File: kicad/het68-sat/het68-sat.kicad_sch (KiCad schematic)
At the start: 10 parts, among them J1 RJ45, U1 AP2112K-1.8

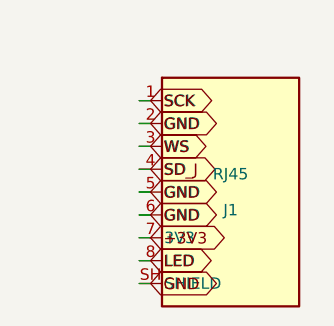
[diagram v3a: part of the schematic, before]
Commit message: Shrink the acoustic board and ground the cable shield only at the HAT.
The HAT outline is 94 by 96 mm and the satellite shell pin is open. The README drops the power-board LED note and estimates a self-built Pico Plus 2 W against the bought module.

Co-authored-by: Cursor <cursoragent@cursor.com>
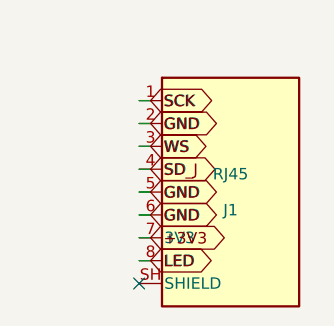
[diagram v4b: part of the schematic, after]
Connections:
- net GND: no longer J1.SH (SHIELD)
- no-connect marks 4 -> 5
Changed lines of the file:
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@@
     (property "Datasheet" "" (at 20 30 0) (effects (font (size 1.27 1.27)) (hide yes)))
     (pin "1")
-    (instances (project "het68-sat" (path "/bc35c63d-5e56-4895-a755-860cebd8b63c" (reference "#PWR00") (unit 1))))
+    (instances (project "het68-sat" (path "/c4451ac6-91a4-4f15-b70a-fef6d342434a" (reference "#PWR00") (unit 1))))
   )
   (global_label "GND"
@@
     (property "Datasheet" "" (at 20 45 0) (effects (font (size 1.27 1.27)) (hide yes)))
     (pin "1")
-    (instances (project "het68-sat" (path "/bc35c63d-5e56-4895-a755-860cebd8b63c" (reference "#PWR01") (unit 1))))
+    (instances (project "het68-sat" (path "/c4451ac6-91a4-4f15-b70a-fef6d342434a" (reference "#PWR01") (unit 1))))
   )
   (global_label "+3V3A"
@@
     (property "Datasheet" "" (at 20 60 0) (effects (font (size 1.27 1.27)) (hide yes)))
     (pin "1")
-    (instances (project "het68-sat" (path "/bc35c63d-5e56-4895-a755-860cebd8b63c" (reference "#PWR02") (unit 1))))
+    (instances (project "het68-sat" (path "/c4451ac6-91a4-4f15-b70a-fef6d342434a" (reference "#PWR02") (unit 1))))
   )
   (global_label "VSYS"
@@
     (property "Datasheet" "" (at 20 75 0) (effects (font (size 1.27 1.27)) (hide yes)))
     (pin "1")
-    (instances (project "het68-sat" (path "/bc35c63d-5e56-4895-a755-860cebd8b63c" (reference "#PWR03") (unit 1))))
+    (instances (project "het68-sat" (path "/c4451ac6-91a4-4f15-b70a-fef6d342434a" (reference "#PWR03") (unit 1))))
   )
   (global_label "VBUS"
@@
     (property "Datasheet" "" (at 20 90 0) (effects (font (size 1.27 1.27)) (hide yes)))
     (pin "1")
-    (instances (project "het68-sat" (path "/bc35c63d-5e56-4895-a755-860cebd8b63c" (reference "#PWR04") (unit 1))))
+    (instances (project "het68-sat" (path "/c4451ac6-91a4-4f15-b70a-fef6d342434a" (reference "#PWR04") (unit 1))))
   )
   (global_label "+3V3"
@@
     (pin "8")
     (pin "SH")
-    (instances (project "het68-sat" (path "/bc35c63d-5e56-4895-a755-860cebd8b63c" (reference "J1") (unit 1))))
+    (instances (project "het68-sat" (path "/c4451ac6-91a4-4f15-b70a-fef6d342434a" (reference "J1") (unit 1))))
   )
   (wire (pts (xy 29.84 489.84) (xy 31.11 489.84))
@@
     (effects (font (size 1.27 1.27)) (justify left))
   )
-  (wire (pts (xy 29.84 510.16) (xy 31.11 510.16))
-    (stroke (width 0) (type solid)))
-  (global_label "GND"
-    (shape bidirectional)
-    (at 31.11 510.16 0)
-    (effects (font (size 1.27 1.27)) (justify left))
-  )
+  (no_connect (at 29.84 510.16))
   (symbol
     (lib_id "het68:AP2112K-1.8")
@@
     (pin "4")
     (pin "5")
-    (instances (project "het68-sat" (path "/bc35c63d-5e56-4895-a755-860cebd8b63c" (reference "U1") (unit 1))))
+    (instances (project "het68-sat" (path "/c4451ac6-91a4-4f15-b70a-fef6d342434a" (reference "U1") (unit 1))))
   )
   (wire (pts (xy 31.11 459.14) (xy 32.38 459.14))
@@
     (pin "4")
     (pin "5")
-    (instances (project "het68-sat" (path "/bc35c63d-5e56-4895-a755-860cebd8b63c" (reference "MK1") (unit 1))))
+    (instances (project "het68-sat" (path "/c4451ac6-91a4-4f15-b70a-fef6d342434a" (reference "MK1") (unit 1))))
   )
   (wire (pts (xy 31.11 433.52) (xy 32.38 433.52))
@@
     (pin "3")
     (pin "4")
-    (instances (project "het68-sat" (path "/bc35c63d-5e56-4895-a755-860cebd8b63c" (reference "D1") (unit 1))))
+    (instances (project "het68-sat" (path "/c4451ac6-91a4-4f15-b70a-fef6d342434a" (reference "D1") (unit 1))))
   )
   (wire (pts (xy 40.0 402.82) (xy 40.0 404.09))
@@
     (pin "1")
     (pin "2")
-    (instances (project "het68-sat" (path "/bc35c63d-5e56-4895-a755-860cebd8b63c" (reference "C1") (unit 1))))
+    (instances (project "het68-sat" (path "/c4451ac6-91a4-4f15-b70a-fef6d342434a" (reference "C1") (unit 1))))
   )
   (wire (pts (xy 40.0 373.39) (xy 40.0 374.66))
@@
     (pin "1")
     (pin "2")
-    (instances (project "het68-sat" (path "/bc35c63d-5e56-4895-a755-860cebd8b63c" (reference "C2") (unit 1))))
+    (instances (project "het68-sat" (path "/c4451ac6-91a4-4f15-b70a-fef6d342434a" (reference "C2") (unit 1))))
   )
   (wire (pts (xy 40.0 347.77) (xy 40.0 349.04))
@@
     (pin "1")
     (pin "2")
-    (instances (project "het68-sat" (path "/bc35c63d-5e56-4895-a755-860cebd8b63c" (reference "C3") (unit 1))))
+    (instances (project "het68-sat" (path "/c4451ac6-91a4-4f15-b70a-fef6d342434a" (reference "C3") (unit 1))))
   )
   (wire (pts (xy 40.0 322.15) (xy 40.0 323.42))
@@
     (pin "1")
     (pin "2")
-    (instances (project "het68-sat" (path "/bc35c63d-5e56-4895-a755-860cebd8b63c" (reference "C4") (unit 1))))
+    (instances (project "het68-sat" (path "/c4451ac6-91a4-4f15-b70a-fef6d342434a" (reference "C4") (unit 1))))
   )
   (wire (pts (xy 40.0 296.53) (xy 40.0 297.8))
@@
     (pin "1")
     (pin "2")
-    (instances (project "het68-sat" (path "/bc35c63d-5e56-4895-a755-860cebd8b63c" (reference "R1") (unit 1))))
+    (instances (project "het68-sat" (path "/c4451ac6-91a4-4f15-b70a-fef6d342434a" (reference "R1") (unit 1))))
   )
   (wire (pts (xy 40.0 270.91) (xy 40.0 272.18))
@@
     (pin "1")
     (pin "2")
-    (instances (project "het68-sat" (path "/bc35c63d-5e56-4895-a755-860cebd8b63c" (reference "R2") (unit 1))))
+    (instances (project "het68-sat" (path "/c4451ac6-91a4-4f15-b70a-fef6d342434a" (reference "R2") (unit 1))))
   )
   (wire (pts (xy 40.0 245.29) (xy 40.0 246.56))

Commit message: Fit every board on printed.cz prototype: 2-layer, 0603, ENIG.
HAT is 140×140 mm so it routes on two layers without 0402 or BGA; satellite and power use the same stack, drill and finish.

Co-authored-by: Cursor <cursoragent@cursor.com>
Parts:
- C1, C2: footprint Capacitor_SMD:C_0402_1005Metric -> Capacitor_SMD:C_0603_1608Metric; MPN CL05A105KA5NQNC -> CL10A105KA8NNNC
- C3, C4: footprint Capacitor_SMD:C_0402_1005Metric -> Capacitor_SMD:C_0603_1608Metric; MPN CL05B104KB5NNNC -> CL10B104KB8NNNC
- R1: footprint Resistor_SMD:R_0402_1005Metric -> Resistor_SMD:R_0603_1608Metric; MPN RC0402FR-0733RL -> RC0603FR-0733RL
- R2: footprint Resistor_SMD:R_0402_1005Metric -> Resistor_SMD:R_0603_1608Metric; MPN RC0402FR-07100KL -> RC0603FR-07100KL
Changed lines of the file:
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@@
     (property "Datasheet" "" (at 20 30 0) (effects (font (size 1.27 1.27)) (hide yes)))
     (pin "1")
-    (instances (project "het68-sat" (path "/2236da0a-ab6f-4773-9c91-a66ce1ab8b2c" (reference "#PWR00") (unit 1))))
+    (instances (project "het68-sat" (path "/938f7ccd-ed1f-4e5b-b71f-bcb60b7c252a" (reference "#PWR00") (unit 1))))
   )
   (global_label "GND"
@@
     (property "Datasheet" "" (at 20 45 0) (effects (font (size 1.27 1.27)) (hide yes)))
     (pin "1")
-    (instances (project "het68-sat" (path "/2236da0a-ab6f-4773-9c91-a66ce1ab8b2c" (reference "#PWR01") (unit 1))))
+    (instances (project "het68-sat" (path "/938f7ccd-ed1f-4e5b-b71f-bcb60b7c252a" (reference "#PWR01") (unit 1))))
   )
   (global_label "+3V3A"
@@
     (property "Datasheet" "" (at 20 60 0) (effects (font (size 1.27 1.27)) (hide yes)))
     (pin "1")
-    (instances (project "het68-sat" (path "/2236da0a-ab6f-4773-9c91-a66ce1ab8b2c" (reference "#PWR02") (unit 1))))
+    (instances (project "het68-sat" (path "/938f7ccd-ed1f-4e5b-b71f-bcb60b7c252a" (reference "#PWR02") (unit 1))))
   )
   (global_label "VSYS"
@@
     (property "Datasheet" "" (at 20 75 0) (effects (font (size 1.27 1.27)) (hide yes)))
     (pin "1")
-    (instances (project "het68-sat" (path "/2236da0a-ab6f-4773-9c91-a66ce1ab8b2c" (reference "#PWR03") (unit 1))))
+    (instances (project "het68-sat" (path "/938f7ccd-ed1f-4e5b-b71f-bcb60b7c252a" (reference "#PWR03") (unit 1))))
   )
   (global_label "VBUS"
@@
     (property "Datasheet" "" (at 20 90 0) (effects (font (size 1.27 1.27)) (hide yes)))
     (pin "1")
-    (instances (project "het68-sat" (path "/2236da0a-ab6f-4773-9c91-a66ce1ab8b2c" (reference "#PWR04") (unit 1))))
+    (instances (project "het68-sat" (path "/938f7ccd-ed1f-4e5b-b71f-bcb60b7c252a" (reference "#PWR04") (unit 1))))
   )
   (global_label "+3V3"
@@
     (pin "8")
     (pin "SH")
-    (instances (project "het68-sat" (path "/2236da0a-ab6f-4773-9c91-a66ce1ab8b2c" (reference "J1") (unit 1))))
+    (instances (project "het68-sat" (path "/938f7ccd-ed1f-4e5b-b71f-bcb60b7c252a" (reference "J1") (unit 1))))
   )
   (wire (pts (xy 29.84 489.84) (xy 31.11 489.84))
@@
     (pin "4")
     (pin "5")
-    (instances (project "het68-sat" (path "/2236da0a-ab6f-4773-9c91-a66ce1ab8b2c" (reference "U1") (unit 1))))
+    (instances (project "het68-sat" (path "/938f7ccd-ed1f-4e5b-b71f-bcb60b7c252a" (reference "U1") (unit 1))))
   )
   (wire (pts (xy 31.11 459.14) (xy 32.38 459.14))
@@
     (pin "4")
     (pin "5")
-    (instances (project "het68-sat" (path "/2236da0a-ab6f-4773-9c91-a66ce1ab8b2c" (reference "MK1") (unit 1))))
+    (instances (project "het68-sat" (path "/938f7ccd-ed1f-4e5b-b71f-bcb60b7c252a" (reference "MK1") (unit 1))))
   )
   (wire (pts (xy 31.11 433.52) (xy 32.38 433.52))
@@
     (pin "3")
     (pin "4")
-    (instances (project "het68-sat" (path "/2236da0a-ab6f-4773-9c91-a66ce1ab8b2c" (reference "D1") (unit 1))))
+    (instances (project "het68-sat" (path "/938f7ccd-ed1f-4e5b-b71f-bcb60b7c252a" (reference "D1") (unit 1))))
   )
   (wire (pts (xy 40.0 402.82) (xy 40.0 404.09))
@@
     (property "Reference" "C1" (at 40.0 379.2 0) (effects (font (size 1.27 1.27))))
     (property "Value" "1u" (at 40.0 375.2 0) (effects (font (size 1.27 1.27))))
-    (property "Footprint" "Capacitor_SMD:C_0402_1005Metric" (at 40.0 377.2 0) (effects (font (size 1.27 1.27)) (hide yes)))
+    (property "Footprint" "Capacitor_SMD:C_0603_1608Metric" (at 40.0 377.2 0) (effects (font (size 1.27 1.27)) (hide yes)))
     (property "Datasheet" "" (at 40.0 377.2 0) (effects (font (size 1.27 1.27)) (hide yes)))
-    (property "MPN" "CL05A105KA5NQNC" (at 40.0 377.2 0) (effects (font (size 1.27 1.27)) (hide yes)))
-    (pin "1")
-    (pin "2")
-    (instances (project "het68-sat" (path "/2236da0a-ab6f-4773-9c91-a66ce1ab8b2c" (reference "C1") (unit 1))))
+    (property "MPN" "CL10A105KA8NNNC" (at 40.0 377.2 0) (effects (font (size 1.27 1.27)) (hide yes)))
+    (pin "1")
+    (pin "2")
+    (instances (project "het68-sat" (path "/938f7ccd-ed1f-4e5b-b71f-bcb60b7c252a" (reference "C1") (unit 1))))
   )
   (wire (pts (xy 40.0 373.39) (xy 40.0 374.66))
@@
     (property "Reference" "C2" (at 40.0 353.58 0) (effects (font (size 1.27 1.27))))
     (property "Value" "1u" (at 40.0 349.58 0) (effects (font (size 1.27 1.27))))
-    (property "Footprint" "Capacitor_SMD:C_0402_1005Metric" (at 40.0 351.58 0) (effects (font (size 1.27 1.27)) (hide yes)))
+    (property "Footprint" "Capacitor_SMD:C_0603_1608Metric" (at 40.0 351.58 0) (effects (font (size 1.27 1.27)) (hide yes)))
     (property "Datasheet" "" (at 40.0 351.58 0) (effects (font (size 1.27 1.27)) (hide yes)))
-    (property "MPN" "CL05A105KA5NQNC" (at 40.0 351.58 0) (effects (font (size 1.27 1.27)) (hide yes)))
-    (pin "1")
-    (pin "2")
-    (instances (project "het68-sat" (path "/2236da0a-ab6f-4773-9c91-a66ce1ab8b2c" (reference "C2") (unit 1))))
+    (property "MPN" "CL10A105KA8NNNC" (at 40.0 351.58 0) (effects (font (size 1.27 1.27)) (hide yes)))
+    (pin "1")
+    (pin "2")
+    (instances (project "het68-sat" (path "/938f7ccd-ed1f-4e5b-b71f-bcb60b7c252a" (reference "C2") (unit 1))))
   )
   (wire (pts (xy 40.0 347.77) (xy 40.0 349.04))
@@
     (property "Reference" "C3" (at 40.0 327.96 0) (effects (font (size 1.27 1.27))))
     (property "Value" "100n" (at 40.0 323.96 0) (effects (font (size 1.27 1.27))))
-    (property "Footprint" "Capacitor_SMD:C_0402_1005Metric" (at 40.0 325.96 0) (effects (font (size 1.27 1.27)) (hide yes)))
+    (property "Footprint" "Capacitor_SMD:C_0603_1608Metric" (at 40.0 325.96 0) (effects (font (size 1.27 1.27)) (hide yes)))
     (property "Datasheet" "" (at 40.0 325.96 0) (effects (font (size 1.27 1.27)) (hide yes)))
-    (property "MPN" "CL05B104KB5NNNC" (at 40.0 325.96 0) (effects (font (size 1.27 1.27)) (hide yes)))
-    (pin "1")
-    (pin "2")
-    (instances (project "het68-sat" (path "/2236da0a-ab6f-4773-9c91-a66ce1ab8b2c" (reference "C3") (unit 1))))
+    (property "MPN" "CL10B104KB8NNNC" (at 40.0 325.96 0) (effects (font (size 1.27 1.27)) (hide yes)))
+    (pin "1")
+    (pin "2")
+    (instances (project "het68-sat" (path "/938f7ccd-ed1f-4e5b-b71f-bcb60b7c252a" (reference "C3") (unit 1))))
   )
   (wire (pts (xy 40.0 322.15) (xy 40.0 323.42))
@@
     (property "Reference" "C4" (at 40.0 302.34 0) (effects (font (size 1.27 1.27))))
     (property "Value" "100n" (at 40.0 298.34 0) (effects (font (size 1.27 1.27))))
-    (property "Footprint" "Capacitor_SMD:C_0402_1005Metric" (at 40.0 300.34 0) (effects (font (size 1.27 1.27)) (hide yes)))
+    (property "Footprint" "Capacitor_SMD:C_0603_1608Metric" (at 40.0 300.34 0) (effects (font (size 1.27 1.27)) (hide yes)))
     (property "Datasheet" "" (at 40.0 300.34 0) (effects (font (size 1.27 1.27)) (hide yes)))
-    (property "MPN" "CL05B104KB5NNNC" (at 40.0 300.34 0) (effects (font (size 1.27 1.27)) (hide yes)))
-    (pin "1")
-    (pin "2")
-    (instances (project "het68-sat" (path "/2236da0a-ab6f-4773-9c91-a66ce1ab8b2c" (reference "C4") (unit 1))))
+    (property "MPN" "CL10B104KB8NNNC" (at 40.0 300.34 0) (effects (font (size 1.27 1.27)) (hide yes)))
+    (pin "1")
+    (pin "2")
+    (instances (project "het68-sat" (path "/938f7ccd-ed1f-4e5b-b71f-bcb60b7c252a" (reference "C4") (unit 1))))
   )
   (wire (pts (xy 40.0 296.53) (xy 40.0 297.8))
@@
     (property "Reference" "R1" (at 40.0 276.71999999999997 0) (effects (font (size 1.27 1.27))))
     (property "Value" "33" (at 40.0 272.71999999999997 0) (effects (font (size 1.27 1.27))))
-    (property "Footprint" "Resistor_SMD:R_0402_1005Metric" (at 40.0 274.71999999999997 0) (effects (font (size 1.27 1.27)) (hide yes)))
+    (property "Footprint" "Resistor_SMD:R_0603_1608Metric" (at 40.0 274.71999999999997 0) (effects (font (size 1.27 1.27)) (hide yes)))
     (property "Datasheet" "" (at 40.0 274.71999999999997 0) (effects (font (size 1.27 1.27)) (hide yes)))
-    (property "MPN" "RC0402FR-0733RL" (at 40.0 274.71999999999997 0) (effects (font (size 1.27 1.27)) (hide yes)))
-    (pin "1")
-    (pin "2")
-    (instances (project "het68-sat" (path "/2236da0a-ab6f-4773-9c91-a66ce1ab8b2c" (reference "R1") (unit 1))))
+    (property "MPN" "RC0603FR-0733RL" (at 40.0 274.71999999999997 0) (effects (font (size 1.27 1.27)) (hide yes)))
+    (pin "1")
+    (pin "2")
+    (instances (project "het68-sat" (path "/938f7ccd-ed1f-4e5b-b71f-bcb60b7c252a" (reference "R1") (unit 1))))
   )
   (wire (pts (xy 40.0 270.91) (xy 40.0 272.18))
@@
     (property "Reference" "R2" (at 40.0 251.09999999999997 0) (effects (font (size 1.27 1.27))))
     (property "Value" "100k" (at 40.0 247.09999999999997 0) (effects (font (size 1.27 1.27))))
-    (property "Footprint" "Resistor_SMD:R_0402_1005Metric" (at 40.0 249.09999999999997 0) (effects (font (size 1.27 1.27)) (hide yes)))
+    (property "Footprint" "Resistor_SMD:R_0603_1608Metric" (at 40.0 249.09999999999997 0) (effects (font (size 1.27 1.27)) (hide yes)))
     (property "Datasheet" "" (at 40.0 249.09999999999997 0) (effects (font (size 1.27 1.27)) (hide yes)))
-    (property "MPN" "RC0402FR-07100KL" (at 40.0 249.09999999999997 0) (effects (font (size 1.27 1.27)) (hide yes)))
-    (pin "1")
-    (pin "2")
-    (instances (project "het68-sat" (path "/2236da0a-ab6f-4773-9c91-a66ce1ab8b2c" (reference "R2") (unit 1))))
+    (property "MPN" "RC0603FR-07100KL" (at 40.0 249.09999999999997 0) (effects (font (size 1.27 1.27)) (hide yes)))
+    (pin "1")
+    (pin "2")
+    (instances (project "het68-sat" (path "/938f7ccd-ed1f-4e5b-b71f-bcb60b7c252a" (reference "R2") (unit 1))))
   )
   (wire (pts (xy 40.0 245.29) (xy 40.0 246.56))

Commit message: Freeze v4 as a native RP2350B 6-layer core with a swappable CT-secondary power board.
MeshCore stays on Heltec V3 via J_MESH so the node remains in the mesh while DSP sleeps; satellites move to LVDS, and mains voltage never lands on copper.

Co-authored-by: Cursor <cursoragent@cursor.com>
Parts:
- removed D1: SK6812, LED_SMD:LED_WS2812B_PLCC4_5.0x5.0mm_P3.2mm, symbol LED:WS2812B
- removed J1: RJ45, Connector_RJ:RJ45_Amphenol_RJHSE5380, symbol het68:RJ45_T568B
- removed R2: 100k, Resistor_SMD:R_0603_1608Metric, symbol Device:R
- removed U1: AP2112K-1.8, Package_TO_SOT_SMD:SOT-23-5, symbol het68:AP2112K-1.8
- added C5: 100n, Capacitor_SMD:C_0603_1608Metric, symbol Device:C
- added D1, D2, D3: PESD5V0X1BT, Diode_SMD:D_SOD-323, symbol Device:D_TVS
- added D4: SK6812, LED_SMD:LED_WS2812B_PLCC4_5.0x5.0mm_P3.2mm, symbol LED:WS2812B
- added F1: 0.25A, Fuse:Fuse_0603_1608Metric, symbol Device:Polyfuse
- added FL1, FL2, FL3: CMC, Inductor_SMD:L_CommonModeChoke_Coilank_ACM2012, symbol het68:CMC
- added J1: RJ45, het68:RJ45_RJHSE5380_het68, symbol het68:RJ45_LVDS
- added U1: AP2112K-1.8, Package_TO_SOT_SMD:SOT-23-5, symbol het68:AP2112K
- added U2, U3: SN65LVDS2, Package_TO_SOT_SMD:SOT-23-5, symbol het68:SN65LVDS2
- added U4: SN65LVDS1, Package_TO_SOT_SMD:SOT-23-5, symbol het68:SN65LVDS1
- added U5: TXS0104E, Package_SO:SOIC-14_3.9x8.7mm_P1.27mm, symbol het68:TXS0104E
- R1: value 33 -> 100k; MPN RC0603FR-0733RL -> RC0603FR-07100KL
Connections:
- net SD_J is gone; now on net GND: R1.2
- net +1V8: now also U1.5 (VOUT), U5.1 (VCCA)
- net +3V3: now also C5.1, D4.1 (VDD), F1.2, U1.1 (VIN), U1.3 (EN), U2.1 (VCC), U3.1 (VCC), U4.5 (VCC), U5.14 (VCCB), U5.8 (OE)
- net GND: now also C5.2, D4.3 (VSS), U1.2 (GND), U2.4 (GND), U3.4 (GND), U4.2 (GND), U5.7 (GND)
- net LED: now also D4.4 (DIN), J1.8 (LED)
- net SCK: now also U5.2 (A1)
- net SD: now also U5.4 (A3)
- net WS: now also U5.3 (A2)
- new net 3V3_F: F1.1, J1.7 (3V3)
- new net SCK_3V3: U2.5 (ROUT), U5.12 (B1)
- new net SCK_N: D1.2 (A2), FL1.3, U2.3 (RIN_N)
- new net SCK_NJ: FL1.2, J1.2 (SCK_N)
- new net SCK_P: D1.1 (A1), FL1.4, U2.2 (RIN_P)
- new net SCK_PJ: FL1.1, J1.1 (SCK_P)
- new net SD_3V3: U4.1 (DIN), U5.10 (B3)
- new net SD_N: D3.2 (A2), FL3.3, U4.4 (Z)
- new net SD_NJ: FL3.2, J1.5 (SD_N)
- new net SD_P: D3.1 (A1), FL3.4, U4.3 (Y)
- new net SD_PJ: FL3.1, J1.4 (SD_P)
- new net WS_3V3: U3.5 (ROUT), U5.11 (B2)
- new net WS_N: D2.2 (A2), FL2.3, U3.3 (RIN_N)
- new net WS_NJ: FL2.2, J1.6 (WS_N)
- new net WS_P: D2.1 (A1), FL2.4, U3.2 (RIN_P)
- new net WS_PJ: FL2.1, J1.3 (WS_P)
- no-connect marks 5 -> 9
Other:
- title: het68 satelit mikrofonu + LED -> het68 satelit LVDS + T5848 + RGB 3.3V

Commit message: Give the satellite the same 6-layer Faraday stack as Core and an 8-LED ring.
Mic data sat→Core already uses SN65LVDS1 into SN65LVDS32; SCK/WS stay LVDS the other way.

Co-authored-by: Cursor <cursoragent@cursor.com>
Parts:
- added C_L1, C_L2, C_L3, C_L4, C_L5, C_L6, C_L7, C_L8: 100n, Capacitor_SMD:C_0603_1608Metric, symbol Device:C
- added D10, D11, D5, D6, D7, D8, D9: SK6812, LED_SMD:LED_WS2812B_PLCC4_5.0x5.0mm_P3.2mm, symbol LED:WS2812B
- F1: value 0.25A -> 0.5A
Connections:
- net +3V3: now also C_L1.1, C_L2.1, C_L3.1, C_L4.1, C_L5.1, C_L6.1, C_L7.1, C_L8.1, D10.1 (VDD), D11.1 (VDD), D5.1 (VDD), D6.1 (VDD), D7.1 (VDD), D8.1 (VDD), D9.1 (VDD)
- net GND: now also C_L1.2, C_L2.2, C_L3.2, C_L4.2, C_L5.2, C_L6.2, C_L7.2, C_L8.2, D10.3 (VSS), D11.3 (VSS), D5.3 (VSS), D6.3 (VSS), D7.3 (VSS), D8.3 (VSS), D9.3 (VSS)
- net LED2: now reaches D4.2 (DOUT)
- net LED2: now also D5.4 (DIN)
- new net LED3: D5.2 (DOUT), D6.4 (DIN)
- new net LED4: D6.2 (DOUT), D7.4 (DIN)
- new net LED5: D7.2 (DOUT), D8.4 (DIN)
- new net LED6: D8.2 (DOUT), D9.4 (DIN)
- new net LED7: D10.4 (DIN), D9.2 (DOUT)
- new net LED8: D10.2 (DOUT), D11.4 (DIN)
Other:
- title: het68 satelit LVDS + T5848 + RGB 3.3V -> het68 satelit 6L LVDS + T5848 + 8x SK6812
